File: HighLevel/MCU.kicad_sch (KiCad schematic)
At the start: 13 parts, among them U2 STM32F40X_LQFP64

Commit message: high level stuff
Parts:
- U1: renamed from U2; value STM32F40X_LQFP64 -> STM32F405RGTx
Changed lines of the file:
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@@
     (pin "1")
     (instances
-      (project "MCU"
-        (path "/f67b84bb-fc24-4057-a4d1-5dd671e1b3ff"
+      (project "HighLevel"
+        (path "/26149e3f-2822-4531-a73b-0a61b71078cc/805b2797-9011-4004-9ce6-542e3355d0ef"
           (reference "#PWR08") (unit 1)
         )
       )
+      (project "MCU"
+        (path "/f67b84bb-fc24-4057-a4d1-5dd671e1b3ff"
+          (reference "#PWR08") (unit 1)
+        )
+      )
     )
   )
@@
     (pin "1")
     (instances
-      (project "MCU"
-        (path "/f67b84bb-fc24-4057-a4d1-5dd671e1b3ff"
+      (project "HighLevel"
+        (path "/26149e3f-2822-4531-a73b-0a61b71078cc/805b2797-9011-4004-9ce6-542e3355d0ef"
           (reference "#PWR03") (unit 1)
         )
       )
+      (project "MCU"
+        (path "/f67b84bb-fc24-4057-a4d1-5dd671e1b3ff"
+          (reference "#PWR03") (unit 1)
+        )
+      )
     )
   )
@@
     (pin "2")
     (instances
-      (project "MCU"
-        (path "/f67b84bb-fc24-4057-a4d1-5dd671e1b3ff"
+      (project "HighLevel"
+        (path "/26149e3f-2822-4531-a73b-0a61b71078cc/805b2797-9011-4004-9ce6-542e3355d0ef"
           (reference "C4") (unit 1)
         )
       )
+      (project "MCU"
+        (path "/f67b84bb-fc24-4057-a4d1-5dd671e1b3ff"
+          (reference "C4") (unit 1)
+        )
+      )
     )
   )
@@
     (pin "1")
     (instances
-      (project "MCU"
-        (path "/f67b84bb-fc24-4057-a4d1-5dd671e1b3ff"
+      (project "HighLevel"
+        (path "/26149e3f-2822-4531-a73b-0a61b71078cc/805b2797-9011-4004-9ce6-542e3355d0ef"
           (reference "#PWR05") (unit 1)
         )
       )
+      (project "MCU"
+        (path "/f67b84bb-fc24-4057-a4d1-5dd671e1b3ff"
+          (reference "#PWR05") (unit 1)
+        )
+      )
     )
   )
@@
     (pin "2")
     (instances
-      (project "MCU"
-        (path "/f67b84bb-fc24-4057-a4d1-5dd671e1b3ff"
+      (project "HighLevel"
+        (path "/26149e3f-2822-4531-a73b-0a61b71078cc/805b2797-9011-4004-9ce6-542e3355d0ef"
           (reference "C12") (unit 1)
         )
       )
+      (project "MCU"
+        (path "/f67b84bb-fc24-4057-a4d1-5dd671e1b3ff"
+          (reference "C12") (unit 1)
+        )
+      )
     )
   )
@@
     (pin "2")
     (instances
-      (project "MCU"
-        (path "/f67b84bb-fc24-4057-a4d1-5dd671e1b3ff"
+      (project "HighLevel"
+        (path "/26149e3f-2822-4531-a73b-0a61b71078cc/805b2797-9011-4004-9ce6-542e3355d0ef"
           (reference "C11") (unit 1)
         )
       )
+      (project "MCU"
+        (path "/f67b84bb-fc24-4057-a4d1-5dd671e1b3ff"
+          (reference "C11") (unit 1)
+        )
+      )
     )
   )
@@
     (pin "2")
     (instances
-      (project "MCU"
-        (path "/f67b84bb-fc24-4057-a4d1-5dd671e1b3ff"
+      (project "HighLevel"
+        (path "/26149e3f-2822-4531-a73b-0a61b71078cc/805b2797-9011-4004-9ce6-542e3355d0ef"
           (reference "C6") (unit 1)
         )
       )
+      (project "MCU"
+        (path "/f67b84bb-fc24-4057-a4d1-5dd671e1b3ff"
+          (reference "C6") (unit 1)
+        )
+      )
     )
   )
@@
     (pin "2")
     (instances
-      (project "MCU"
-        (path "/f67b84bb-fc24-4057-a4d1-5dd671e1b3ff"
+      (project "HighLevel"
+        (path "/26149e3f-2822-4531-a73b-0a61b71078cc/805b2797-9011-4004-9ce6-542e3355d0ef"
           (reference "C10") (unit 1)
         )
       )
+      (project "MCU"
+        (path "/f67b84bb-fc24-4057-a4d1-5dd671e1b3ff"
+          (reference "C10") (unit 1)
+        )
+      )
     )
   )
   (symbol (lib_id "MCU_ST_STM32F4:STM32F405RGTx") (at 171.45 88.9 0) (unit 1)
     (in_bom yes) (on_board yes) (dnp no) (fields_autoplaced)
-    (property "Reference" "U2" (at 175.9459 134.62 0)
-      (effects (font (size 1.27 1.27)) (justify left))
-    )
-    (property "Value" "STM32F40X_LQFP64" (at 175.9459 137.16 0)
+    (property "Reference" "U1" (at 175.9459 134.62 0)
+      (effects (font (size 1.27 1.27)) (justify left))
+    )
+    (property "Value" "STM32F405RGTx" (at 175.9459 137.16 0)
       (effects (font (size 1.27 1.27)) (justify left))
     )
@@
     (pin "9")
     (instances
-      (project "MCU"
-        (path "/f67b84bb-fc24-4057-a4d1-5dd671e1b3ff"
-          (reference "U2") (unit 1)
+      (project "HighLevel"
+        (path "/26149e3f-2822-4531-a73b-0a61b71078cc/805b2797-9011-4004-9ce6-542e3355d0ef"
+          (reference "U1") (unit 1)
+        )
+      )
+      (project "MCU"
+        (path "/f67b84bb-fc24-4057-a4d1-5dd671e1b3ff"
+          (reference "U1") (unit 1)
         )
       )
@@
     (pin "2")
     (instances
-      (project "MCU"
-        (path "/f67b84bb-fc24-4057-a4d1-5dd671e1b3ff"
+      (project "HighLevel"
+        (path "/26149e3f-2822-4531-a73b-0a61b71078cc/805b2797-9011-4004-9ce6-542e3355d0ef"
           (reference "C9") (unit 1)
         )
       )
+      (project "MCU"
+        (path "/f67b84bb-fc24-4057-a4d1-5dd671e1b3ff"
+          (reference "C9") (unit 1)
+        )
+      )
     )
   )
@@
     (pin "2")
     (instances
-      (project "MCU"
-        (path "/f67b84bb-fc24-4057-a4d1-5dd671e1b3ff"
+      (project "HighLevel"
+        (path "/26149e3f-2822-4531-a73b-0a61b71078cc/805b2797-9011-4004-9ce6-542e3355d0ef"
           (reference "C13") (unit 1)
         )
       )
+      (project "MCU"
+        (path "/f67b84bb-fc24-4057-a4d1-5dd671e1b3ff"
+          (reference "C13") (unit 1)
+        )
+      )
     )
   )
@@
     (pin "2")
     (instances
-      (project "MCU"
-        (path "/f67b84bb-fc24-4057-a4d1-5dd671e1b3ff"
+      (project "HighLevel"
+        (path "/26149e3f-2822-4531-a73b-0a61b71078cc/805b2797-9011-4004-9ce6-542e3355d0ef"
           (reference "C3") (unit 1)
         )
       )
+      (project "MCU"
+        (path "/f67b84bb-fc24-4057-a4d1-5dd671e1b3ff"
+          (reference "C3") (unit 1)
+        )
+      )
     )
   )
@@
     (pin "1")
     (instances
-      (project "MCU"
-        (path "/f67b84bb-fc24-4057-a4d1-5dd671e1b3ff"
+      (project "HighLevel"
+        (path "/26149e3f-2822-4531-a73b-0a61b71078cc/805b2797-9011-4004-9ce6-542e3355d0ef"
           (reference "#PWR06") (unit 1)
         )
       )
+      (project "MCU"
+        (path "/f67b84bb-fc24-4057-a4d1-5dd671e1b3ff"
+          (reference "#PWR06") (unit 1)
+        )
+      )
     )
   )
@@
     (pin "1")
     (instances
-      (project "MCU"
-        (path "/f67b84bb-fc24-4057-a4d1-5dd671e1b3ff"
+      (project "HighLevel"
+        (path "/26149e3f-2822-4531-a73b-0a61b71078cc/805b2797-9011-4004-9ce6-542e3355d0ef"
           (reference "#PWR04") (unit 1)
         )
       )
+      (project "MCU"
+        (path "/f67b84bb-fc24-4057-a4d1-5dd671e1b3ff"
+          (reference "#PWR04") (unit 1)
+        )
+      )
     )
   )
@@
     (pin "1")
     (instances
-      (project "MCU"
-        (path "/f67b84bb-fc24-4057-a4d1-5dd671e1b3ff"
+      (project "HighLevel"
+        (path "/26149e3f-2822-4531-a73b-0a61b71078cc/805b2797-9011-4004-9ce6-542e3355d0ef"
           (reference "#PWR01") (unit 1)
         )
       )
+      (project "MCU"
+        (path "/f67b84bb-fc24-4057-a4d1-5dd671e1b3ff"
+          (reference "#PWR01") (unit 1)
+        )
+      )
     )
   )
@@
     (pin "1")
     (instances
-      (project "MCU"
-        (path "/f67b84bb-fc24-4057-a4d1-5dd671e1b3ff"
+      (project "HighLevel"
+        (path "/26149e3f-2822-4531-a73b-0a61b71078cc/805b2797-9011-4004-9ce6-542e3355d0ef"
           (reference "#PWR02") (unit 1)
         )
       )
+      (project "MCU"
+        (path "/f67b84bb-fc24-4057-a4d1-5dd671e1b3ff"
+          (reference "#PWR02") (unit 1)
+        )
+      )
     )
   )
@@
     (pin "2")
     (instances
-      (project "MCU"
-        (path "/f67b84bb-fc24-4057-a4d1-5dd671e1b3ff"
+      (project "HighLevel"
+        (path "/26149e3f-2822-4531-a73b-0a61b71078cc/805b2797-9011-4004-9ce6-542e3355d0ef"
           (reference "C8") (unit 1)
         )
       )
+      (project "MCU"
+        (path "/f67b84bb-fc24-4057-a4d1-5dd671e1b3ff"
+          (reference "C8") (unit 1)
+        )
+      )
     )
   )
@@
     (pin "2")
     (instances
-      (project "MCU"
-        (path "/f67b84bb-fc24-4057-a4d1-5dd671e1b3ff"
+      (project "HighLevel"
+        (path "/26149e3f-2822-4531-a73b-0a61b71078cc/805b2797-9011-4004-9ce6-542e3355d0ef"
           (reference "C7") (unit 1)
         )
       )
+      (project "MCU"
+        (path "/f67b84bb-fc24-4057-a4d1-5dd671e1b3ff"
+          (reference "C7") (unit 1)
+        )
+      )
     )
   )
@@
     (pin "1")
     (instances
-      (project "MCU"
-        (path "/f67b84bb-fc24-4057-a4d1-5dd671e1b3ff"
+      (project "HighLevel"
+        (path "/26149e3f-2822-4531-a73b-0a61b71078cc/805b2797-9011-4004-9ce6-542e3355d0ef"
           (reference "#PWR07") (unit 1)
         )
       )
+      (project "MCU"
+        (path "/f67b84bb-fc24-4057-a4d1-5dd671e1b3ff"
+          (reference "#PWR07") (unit 1)
+        )
+      )
     )
   )
@@
     (pin "2")
     (instances
+      (project "HighLevel"
+        (path "/26149e3f-2822-4531-a73b-0a61b71078cc/805b2797-9011-4004-9ce6-542e3355d0ef"
+          (reference "C5") (unit 1)
+        )
+      )
       (project "MCU"
         (path "/f67b84bb-fc24-4057-a4d1-5dd671e1b3ff"
@@
     (pin "4")
     (instances
-      (project "MCU"
-        (path "/f67b84bb-fc24-4057-a4d1-5dd671e1b3ff"
+      (project "HighLevel"
+        (path "/26149e3f-2822-4531-a73b-0a61b71078cc/805b2797-9011-4004-9ce6-542e3355d0ef"
           (reference "Y1") (unit 1)
         )
       )
-    )
-  )
-  (sheet_instances
-    (path "/" (page "1"))
+      (project "MCU"
+        (path "/f67b84bb-fc24-4057-a4d1-5dd671e1b3ff"
+          (reference "Y1") (unit 1)
+        )
+      )
+    )
   )
 )

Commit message: Final High Level + edits + footprint
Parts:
- C10: renamed from C3; footprint (none) -> Capacitor_SMD:C_0805_2012Metric
- C11: renamed from C6; footprint (none) -> Capacitor_SMD:C_0805_2012Metric
- C12: renamed from C7; footprint (none) -> Capacitor_SMD:C_0805_2012Metric
- C13: renamed from C10; footprint (none) -> Capacitor_SMD:C_0805_2012Metric
- C14: renamed from C11; footprint (none) -> Capacitor_SMD:C_0805_2012Metric
- C15: renamed from C12; footprint (none) -> Capacitor_SMD:C_0805_2012Metric
- C16: renamed from C13; footprint (none) -> Capacitor_SMD:C_0805_2012Metric
- C6: renamed from C8; footprint (none) -> Capacitor_SMD:C_0805_2012Metric
- C7: renamed from C9; footprint (none) -> Capacitor_SMD:C_0805_2012Metric
- C8: renamed from C4; footprint (none) -> Capacitor_SMD:C_0805_2012Metric
- C9: renamed from C5; footprint (none) -> Capacitor_SMD:C_0805_2012Metric
- Y1: footprint (none) -> Capacitor_SMD:C_0805_2012Metric
- renumbered U1 to U3

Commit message: Fix all errors
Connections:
- net VCC: now also U3.1 (VBAT), U3.19 (VDD), U3.32 (VDD), U3.48 (VDD), U3.64 (VDD)
- net PC13: now reaches U3.2 (PC13)
- net SPI3_CE: now reaches U3.3 (PC14)
- net SPI3_CSN: now reaches U3.4 (PC15)
- net PC10_UART_TX renamed SPI3_SCK
- net PC12 renamed SPI3_MOSI
- net PX11_UART_RX renamed SPI3_MISO
- net TX_SCK_MOSI: no longer names the net of U3.29 (PB10)
- no-connect marks 8 -> 6
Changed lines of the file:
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@@
   (junction (at 252.73 24.13) (diameter 0) (color 0 0 0 0)
   )
-  (no_connect (at 153.67 101.6))
   (no_connect (at 189.23 99.06))
   (no_connect (at 189.23 83.82))
   (no_connect (at 189.23 93.98))
-  (no_connect (at 153.67 104.14))
+  (no_connect (at 189.23 114.3))
   (no_connect (at 189.23 119.38))
-  (no_connect (at 153.67 106.68))
   (no_connect (at 189.23 96.52))
   (wire (pts (xy 171.45 137.16) (xy 171.45 138.43))
@@
     (stroke (width 0) (type default))
   )
-  (wire (pts (xy 163.83 36.83) (xy 166.37 36.83))
-    (stroke (width 0) (type default))
-  )
   (wire (pts (xy 130.81 62.23) (xy 135.89 62.23))
     (stroke (width 0) (type default))
@@
     (effects (font (size 1.27 1.27)) (justify left))
   )
+  (hierarchical_label "SPI3_MOSI" (shape input) (at 153.67 99.06 180) (fields_autoplaced)
+    (effects (font (size 1.27 1.27)) (justify right))
+  )
   (hierarchical_label "ADC_TEMP" (shape input) (at 189.23 53.34 0) (fields_autoplaced)
     (effects (font (size 1.27 1.27)) (justify left))
@@
     (effects (font (size 1.27 1.27)) (justify left))
   )
-  (hierarchical_label "PX11_UART_RX" (shape input) (at 153.67 96.52 180) (fields_autoplaced)
+  (hierarchical_label "SPI3_MISO" (shape input) (at 153.67 96.52 180) (fields_autoplaced)
     (effects (font (size 1.27 1.27)) (justify right))
   )
@@
     (effects (font (size 1.27 1.27)) (justify left))
   )
+  (hierarchical_label "SPI3_CE" (shape input) (at 153.67 104.14 180) (fields_autoplaced)
+    (effects (font (size 1.27 1.27)) (justify right))
+  )
   (hierarchical_label "L3" (shape output) (at 189.23 127 0) (fields_autoplaced)
     (effects (font (size 1.27 1.27)) (justify left))
@@
     (effects (font (size 1.27 1.27)) (justify right))
   )
+  (hierarchical_label "TX_SCL_MOSI" (shape input) (at 189.23 63.5 0) (fields_autoplaced)
+    (effects (font (size 1.27 1.27)) (justify left))
+  )
   (hierarchical_label "RX_SDA_NSS" (shape input) (at 189.23 55.88 0) (fields_autoplaced)
     (effects (font (size 1.27 1.27)) (justify left))
@@
     (effects (font (size 1.27 1.27)) (justify right))
   )
-  (hierarchical_label "TX_SCK_MOSI" (shape output) (at 189.23 114.3 0) (fields_autoplaced)
-    (effects (font (size 1.27 1.27)) (justify left))
-  )
   (hierarchical_label "USB_DM" (shape bidirectional) (at 189.23 73.66 0) (fields_autoplaced)
     (effects (font (size 1.27 1.27)) (justify left))
@@
     (effects (font (size 1.27 1.27)) (justify left))
   )
+  (hierarchical_label "SPI3_CSN" (shape input) (at 153.67 106.68 180) (fields_autoplaced)
+    (effects (font (size 1.27 1.27)) (justify right))
+  )
   (hierarchical_label "SERVO" (shape output) (at 189.23 104.14 0) (fields_autoplaced)
     (effects (font (size 1.27 1.27)) (justify left))
@@
     (effects (font (size 1.27 1.27)) (justify right))
   )
-  (hierarchical_label "PC12" (shape input) (at 153.67 99.06 180) (fields_autoplaced)
+  (hierarchical_label "PC13" (shape input) (at 153.67 101.6 180) (fields_autoplaced)
     (effects (font (size 1.27 1.27)) (justify right))
   )
@@
     (effects (font (size 1.27 1.27)) (justify left))
   )
-  (hierarchical_label "PC10_UART_TX" (shape input) (at 153.67 93.98 180) (fields_autoplaced)
+  (hierarchical_label "SPI3_SCK" (shape input) (at 153.67 93.98 180) (fields_autoplaced)
     (effects (font (size 1.27 1.27)) (justify right))
   )
@@
     (effects (font (size 1.27 1.27)) (justify left))
   )
-  (hierarchical_label "TX_SCL_MOSI" (shape output) (at 189.23 63.5 0) (fields_autoplaced)
-    (effects (font (size 1.27 1.27)) (justify left))
-  )
   (hierarchical_label "ADC_TEMP3" (shape input) (at 189.23 91.44 0) (fields_autoplaced)
     (effects (font (size 1.27 1.27)) (justify left))
-  )
-  (netclass_flag "" (length 2.54) (shape round) (at 163.83 36.83 90) (fields_autoplaced)
-    (effects (font (size 1.27 1.27)) (justify left bottom))
-    (property "Netclass" "VCC" (at 161.29 36.1315 90)
-      (effects (font (size 1.27 1.27) italic) (justify left))
-    )
   )
   (netclass_flag "" (length 2.54) (shape round) (at 246.38 19.05 0) (fields_autoplaced)
@@
         )
       )
+    )
+  )
+  (symbol (lib_id "power:VCC") (at 166.37 36.83 0) (unit 1)
+    (in_bom yes) (on_board yes) (dnp no) (fields_autoplaced)
+    (property "Reference" "#PWR081" (at 166.37 40.64 0)
+      (effects (font (size 1.27 1.27)) hide)
+    )
+    (property "Value" "VCC" (at 166.37 33.02 0)
+      (effects (font (size 1.27 1.27)))
+    )
+    (property "Footprint" "" (at 166.37 36.83 0)
+      (effects (font (size 1.27 1.27)) hide)
+    )
+    (property "Datasheet" "" (at 166.37 36.83 0)
+      (effects (font (size 1.27 1.27)) hide)
+    )
+    (pin "1")
+    (instances
+      (project "HighLevel"
+        (path "/26149e3f-2822-4531-a73b-0a61b71078cc/805b2797-9011-4004-9ce6-542e3355d0ef"
+          (reference "#PWR081") (unit 1)
+        )
+      )
+      (project "MCU"
+        (path "/f67b84bb-fc24-4057-a4d1-5dd671e1b3ff"
+          (reference "#PWR08") (unit 1)
+        )
+      )

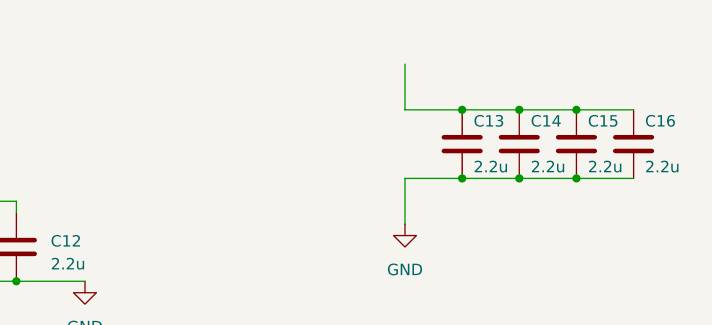
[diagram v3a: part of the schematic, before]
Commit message: Started PCB and added connections to MCU
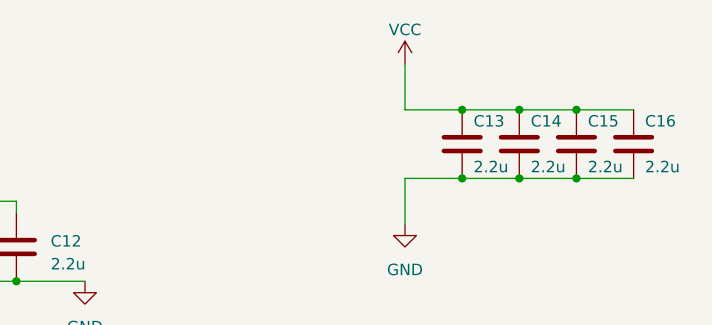
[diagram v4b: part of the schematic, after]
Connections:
- net VCC: now also C13.1, C14.1, C15.1, C16.1
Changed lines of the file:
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@@
     (effects (font (size 1.27 1.27)) (justify left))
-  )
-  (netclass_flag "" (length 2.54) (shape round) (at 246.38 19.05 0) (fields_autoplaced)
-    (effects (font (size 1.27 1.27)) (justify left bottom))
-    (property "Netclass" "VCC" (at 247.0785 16.51 0)
-      (effects (font (size 1.27 1.27) italic) (justify left))
-    )
   )
   (symbol (lib_id "power:VCC") (at 179.07 30.48 0) (unit 1)
@@
         )
       )
+    )
+  )
+  (symbol (lib_id "power:VCC") (at 246.38 19.05 0) (unit 1)
+    (in_bom yes) (on_board yes) (dnp no) (fields_autoplaced)
+    (property "Reference" "#PWR085" (at 246.38 22.86 0)
+      (effects (font (size 1.27 1.27)) hide)
+    )
+    (property "Value" "VCC" (at 246.38 15.24 0)
+      (effects (font (size 1.27 1.27)))
+    )
+    (property "Footprint" "" (at 246.38 19.05 0)
+      (effects (font (size 1.27 1.27)) hide)
+    )
+    (property "Datasheet" "" (at 246.38 19.05 0)
+      (effects (font (size 1.27 1.27)) hide)
+    )
+    (pin "1")
+    (instances
+      (project "HighLevel"
+        (path "/26149e3f-2822-4531-a73b-0a61b71078cc/805b2797-9011-4004-9ce6-542e3355d0ef"
+          (reference "#PWR085") (unit 1)
+        )
+      )
+      (project "MCU"
+        (path "/f67b84bb-fc24-4057-a4d1-5dd671e1b3ff"
+          (reference "#PWR08") (unit 1)
+        )
+      )
